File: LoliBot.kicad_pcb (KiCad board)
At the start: 2 copper layers, 130 x 139.9 mm, 0 parts

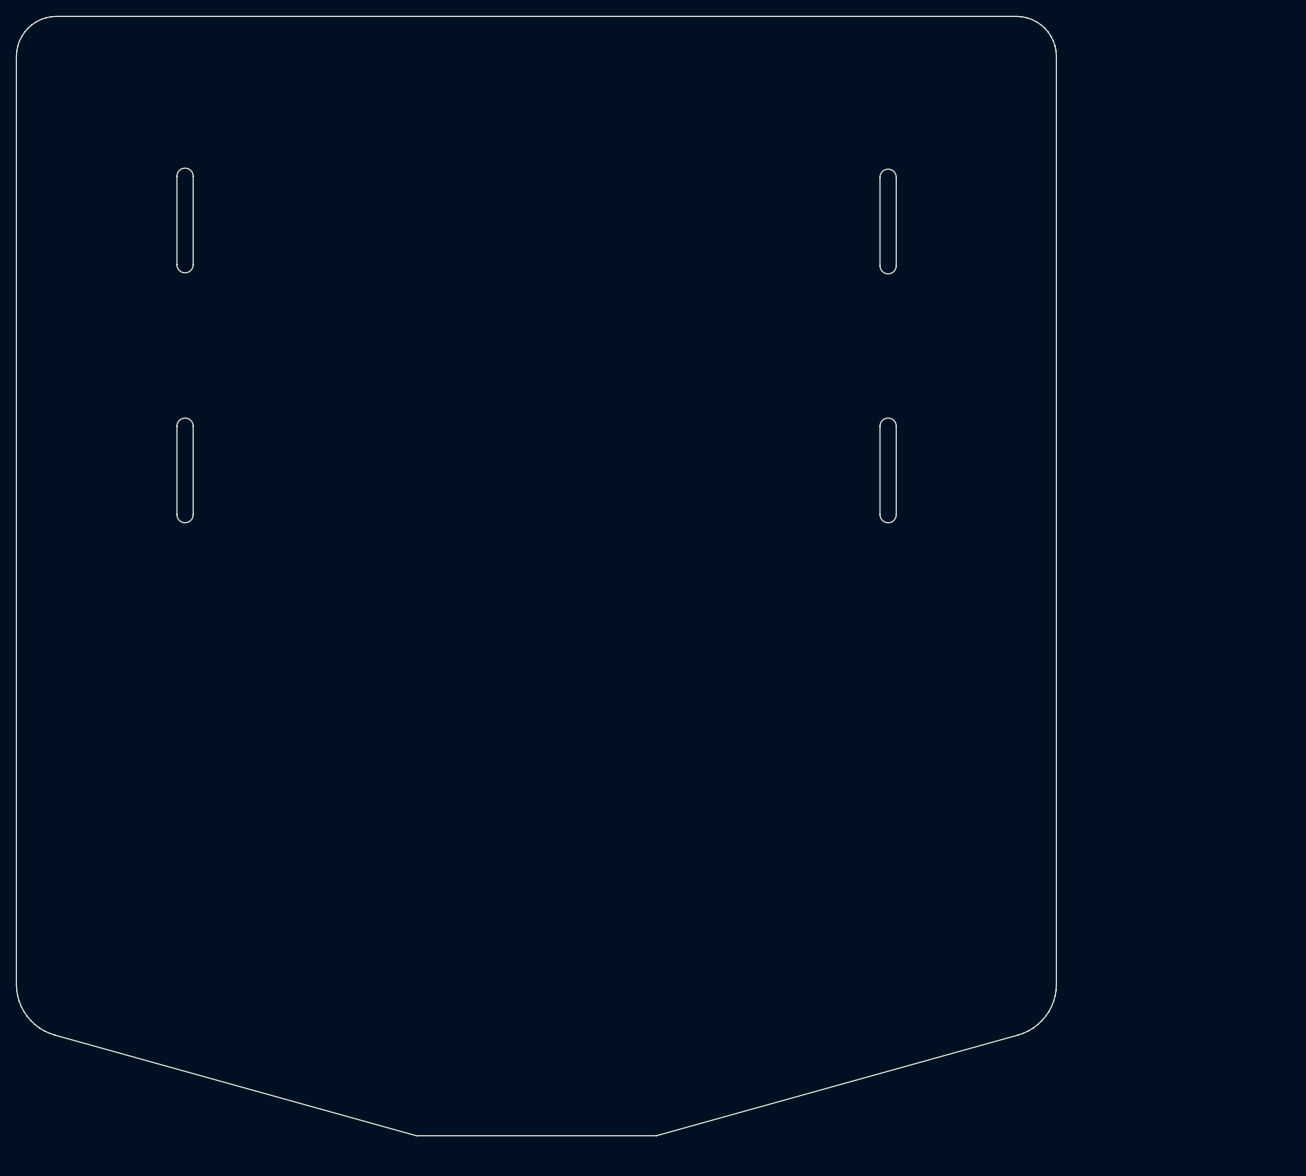
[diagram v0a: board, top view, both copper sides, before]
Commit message: feat(Layout) Added slots and drill holes based on the existing DXF
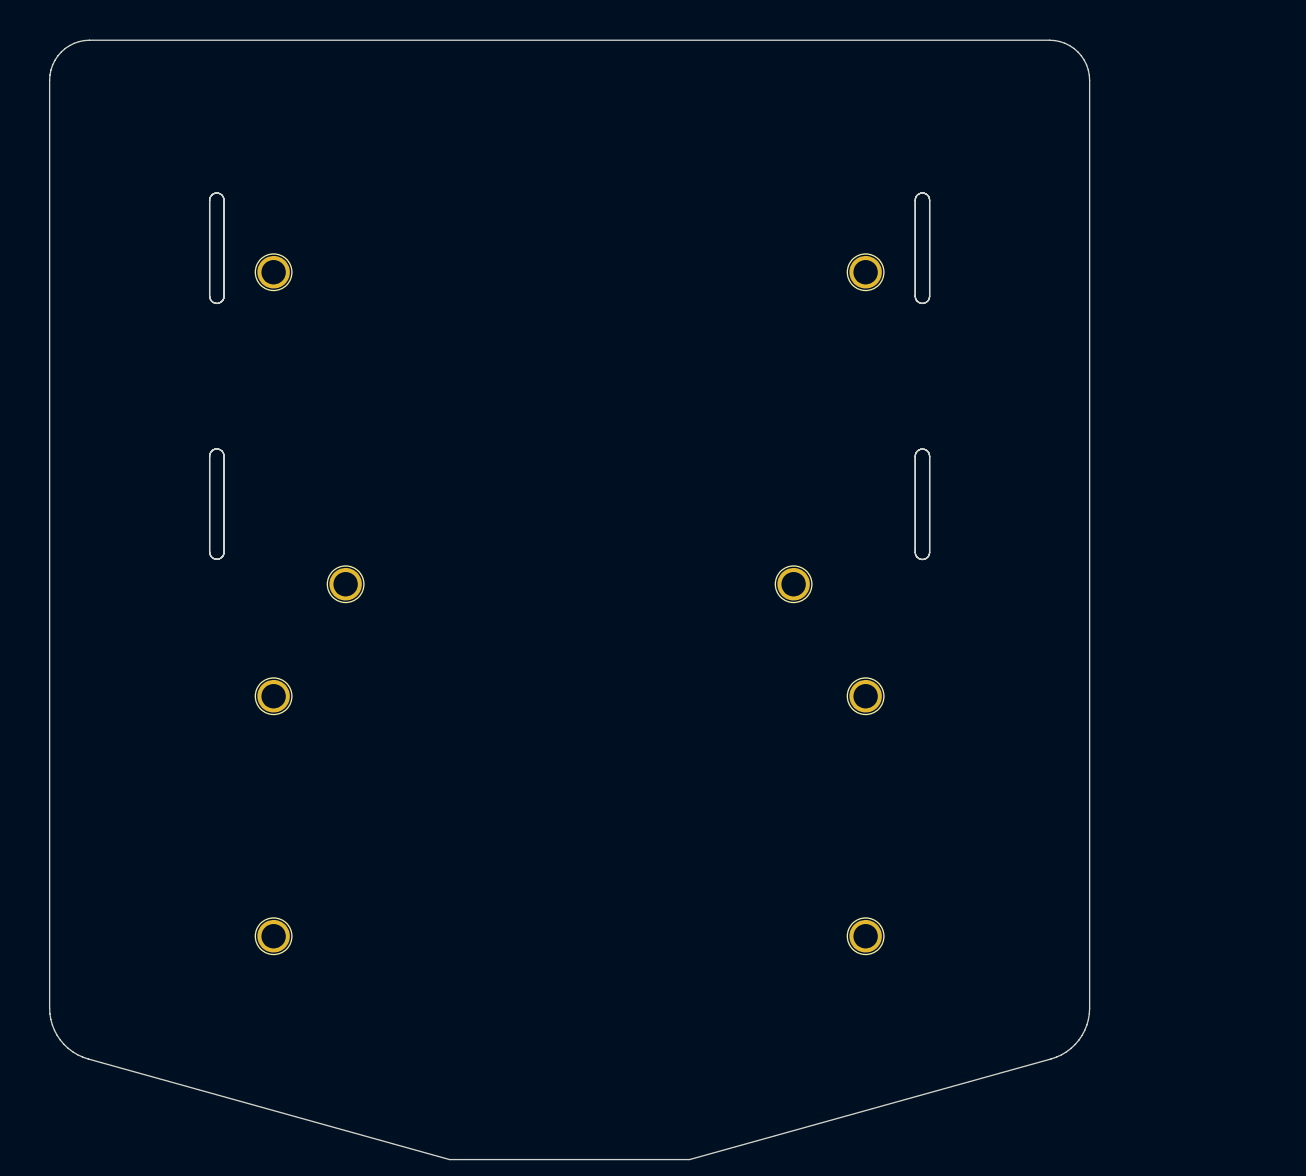
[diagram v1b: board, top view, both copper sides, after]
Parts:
- added REF**: 1pin, Connectors:1pin, F.Cu at (144.0, 143.0)
- added REF**: 1pin, Connectors:1pin, F.Cu at (70.0, 143.0)
- added REF**: 1pin, Connectors:1pin, F.Cu at (144.0, 113.0)
- added REF**: 1pin, Connectors:1pin, F.Cu at (70.0, 113.0)
- added REF**: 1pin, Connectors:1pin, F.Cu at (79.0, 99.0)
- added REF**: 1pin, Connectors:1pin, F.Cu at (135.0, 99.0)
- added REF**: 1pin, Connectors:1pin, F.Cu at (144.0, 60.0)
- added REF**: 1pin, Connectors:1pin, F.Cu at (70.0, 60.0)
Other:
- outline, holes or cut-outs redrawn

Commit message: Added Board for JS Version
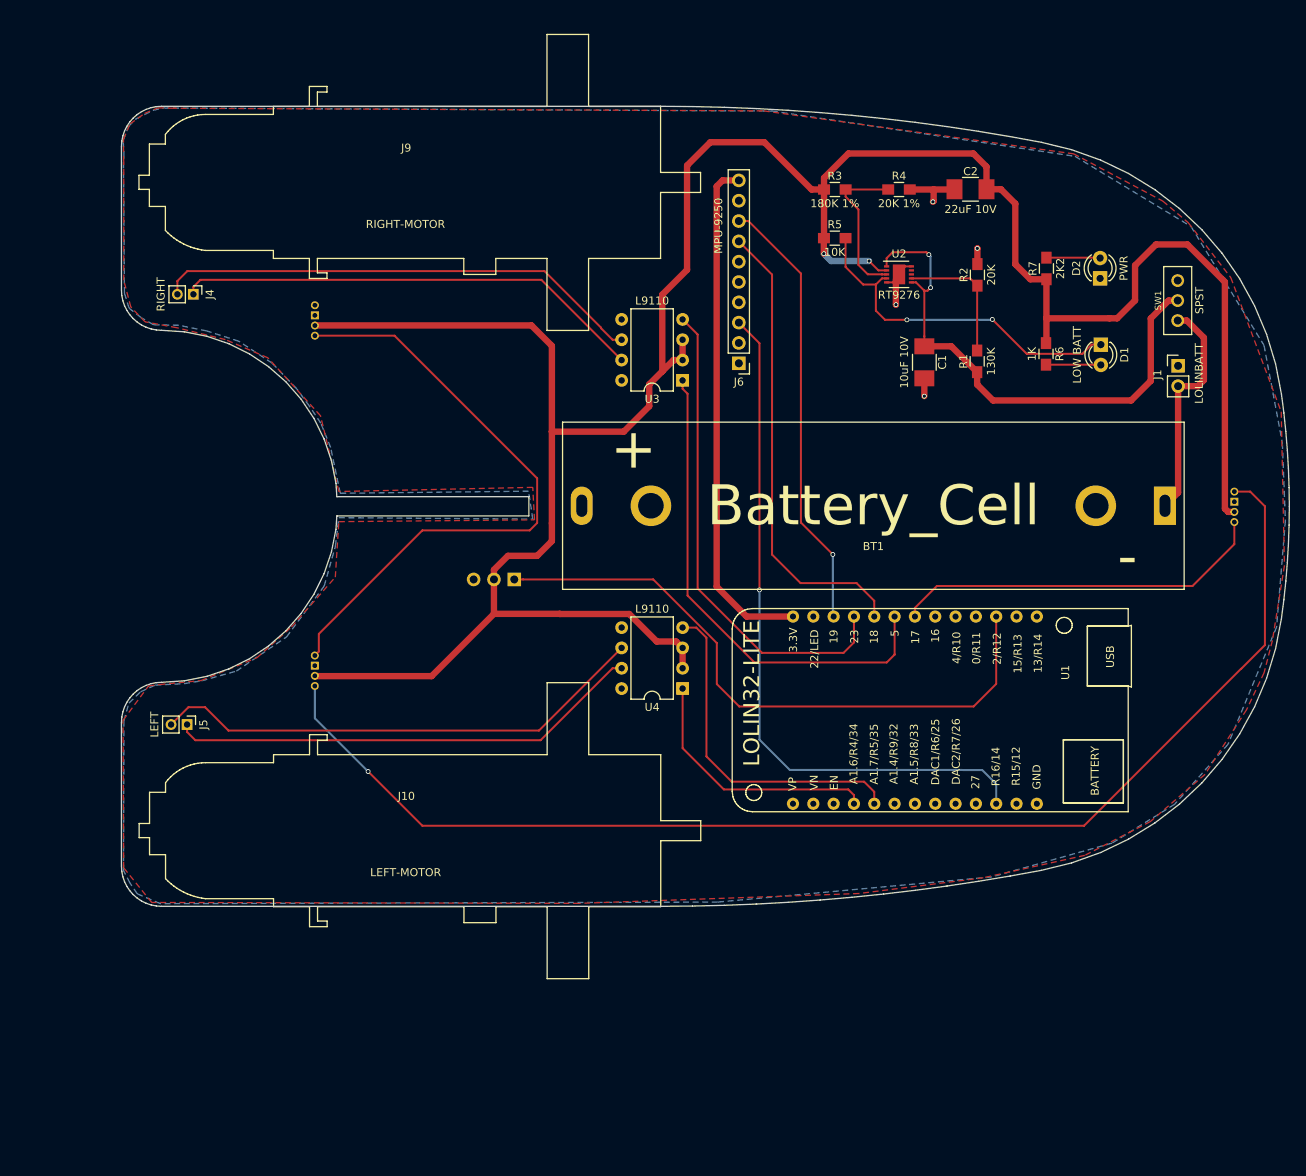
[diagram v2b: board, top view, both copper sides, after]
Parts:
- removed REF** (x8): 1pin, Connectors:1pin
- added BT1: Battery_Cell, libs:BH-18650, F.Cu at (145.0, 89.2)
- added C1: 10uF 10V, Capacitors_SMD:C_1210_HandSoldering, F.Cu at (151.3, 71.3)
- added C2: 22uF 10V, Capacitors_SMD:C_1210_HandSoldering, F.Cu at (157.1, 49.6)
- added D1: LOW BATT, LEDs:LED_D3.0mm, F.Cu at (173.4, 69.0)
- added D2: PWR, LEDs:LED_D3.0mm, F.Cu at (173.3, 60.8)
- added J1: LOLINBATT, Pin_Headers:Pin_Header_Straight_1x02_Pitch2.54mm, F.Cu at (183.1, 71.7)
- added J10: LEFT-MOTOR, libs:DC-Motor, F.Cu at (86.5, 129.9)
- added J2: APA106, libs:LED_8MM_APA-106, B.Cu at (190.1, 89.3)
- added J3: SERVO1, Pin_Headers:Pin_Header_Straight_1x03_Pitch2.54mm, B.Cu at (100.1, 98.4)
- added J4: RIGHT, Pin_Headers:Pin_Header_Straight_1x02_Pitch2.00mm, F.Cu at (60.0, 62.8)
- added J5: LEFT, Pin_Headers:Pin_Header_Straight_1x02_Pitch2.00mm, F.Cu at (59.2, 116.5)
- added J6: MPU-9250, Pin_Headers:Pin_Header_Straight_1x10_Pitch2.54mm, F.Cu at (128.2, 71.4)
- added J7: APA106, libs:LED_8MM_APA-106, B.Cu at (75.2, 109.8)
- added J8: APA106, libs:LED_8MM_APA-106, B.Cu at (75.2, 66.0)
- added J9: RIGHT-MOTOR, libs:DC-Motor, F.Cu at (86.5, 48.9)
- added R1: 130K, Resistors_SMD:R_0805_HandSoldering, F.Cu at (157.9, 71.1)
- added R2: 20K, Resistors_SMD:R_0805_HandSoldering, F.Cu at (158.0, 60.3)
- added R3: 180K 1%, Resistors_SMD:R_0805_HandSoldering, F.Cu at (140.2, 49.7)
- added R4: 20K 1%, Resistors_SMD:R_0805_HandSoldering, F.Cu at (148.2, 49.7)
- added R5: 10K, Resistors_SMD:R_0805_HandSoldering, F.Cu at (140.1, 55.7)
- added R6: 1K, Resistors_SMD:R_0805_HandSoldering, F.Cu at (166.6, 70.2)
- added R7: 2K2, Resistors_SMD:R_0805_HandSoldering, F.Cu at (166.6, 59.5)
- added SW1: SPST, libs:SS12D00, F.Cu at (183.0, 63.5)
- added U1: LOLIN32-LITE, libs:lolin32-lite, F.Cu at (153.3, 114.7)
- added U2: RT9276, Housings_DFN_QFN:DFN-10-1EP_3x3mm_Pitch0.5mm, F.Cu at (148.2, 60.3)
- added U3: L9110, Housings_DIP:DIP-8_W7.62mm, F.Cu at (121.1, 73.5)
- added U4: L9110, Housings_DIP:DIP-8_W7.62mm, F.Cu at (121.1, 112.0)
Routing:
- net +5V: track 0.00 -> 322.8 mm, vias 0 -> 2
- net Net-(J2-Pad4): track 0.00 -> 159.6 mm, vias 0 -> 1
- net /INT: track 0.00 -> 87.5 mm, vias 0 -> 1
- net /IO2: track 0.00 -> 79.4 mm
- net Net-(J7-Pad4): track 0.00 -> 76.7 mm
- net Net-(C1-Pad1): track 0.00 -> 66.1 mm, vias 0 -> 2
- net +3V3: track 0.00 -> 64.2 mm
- net Net-(J5-Pad2): track 0.00 -> 62.7 mm
- net /IO5: track 0.00 -> 61.7 mm
- net Net-(J4-Pad2): track 0.00 -> 61.3 mm
- net /IO23: track 0.00 -> 61.1 mm
- net Net-(J5-Pad1): track 0.00 -> 59.4 mm
- net Net-(J4-Pad1): track 0.00 -> 59.0 mm
- net /IO18: track 0.00 -> 58.0 mm
- net /IO19: track 0.00 -> 55.1 mm, vias 0 -> 1
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- added copper zone on B.Cu, net GND
- added copper zone on F.Cu, net GND
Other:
- board size 130 x 139.9 mm -> 146 x 100 mm
